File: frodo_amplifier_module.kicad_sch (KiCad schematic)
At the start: 38 parts, among them IC1 INA826AID, U1 ADC101C021CIMM, U2 MCP6001-OT, U3 MIC5504-3.3YM5, U4 REF3033

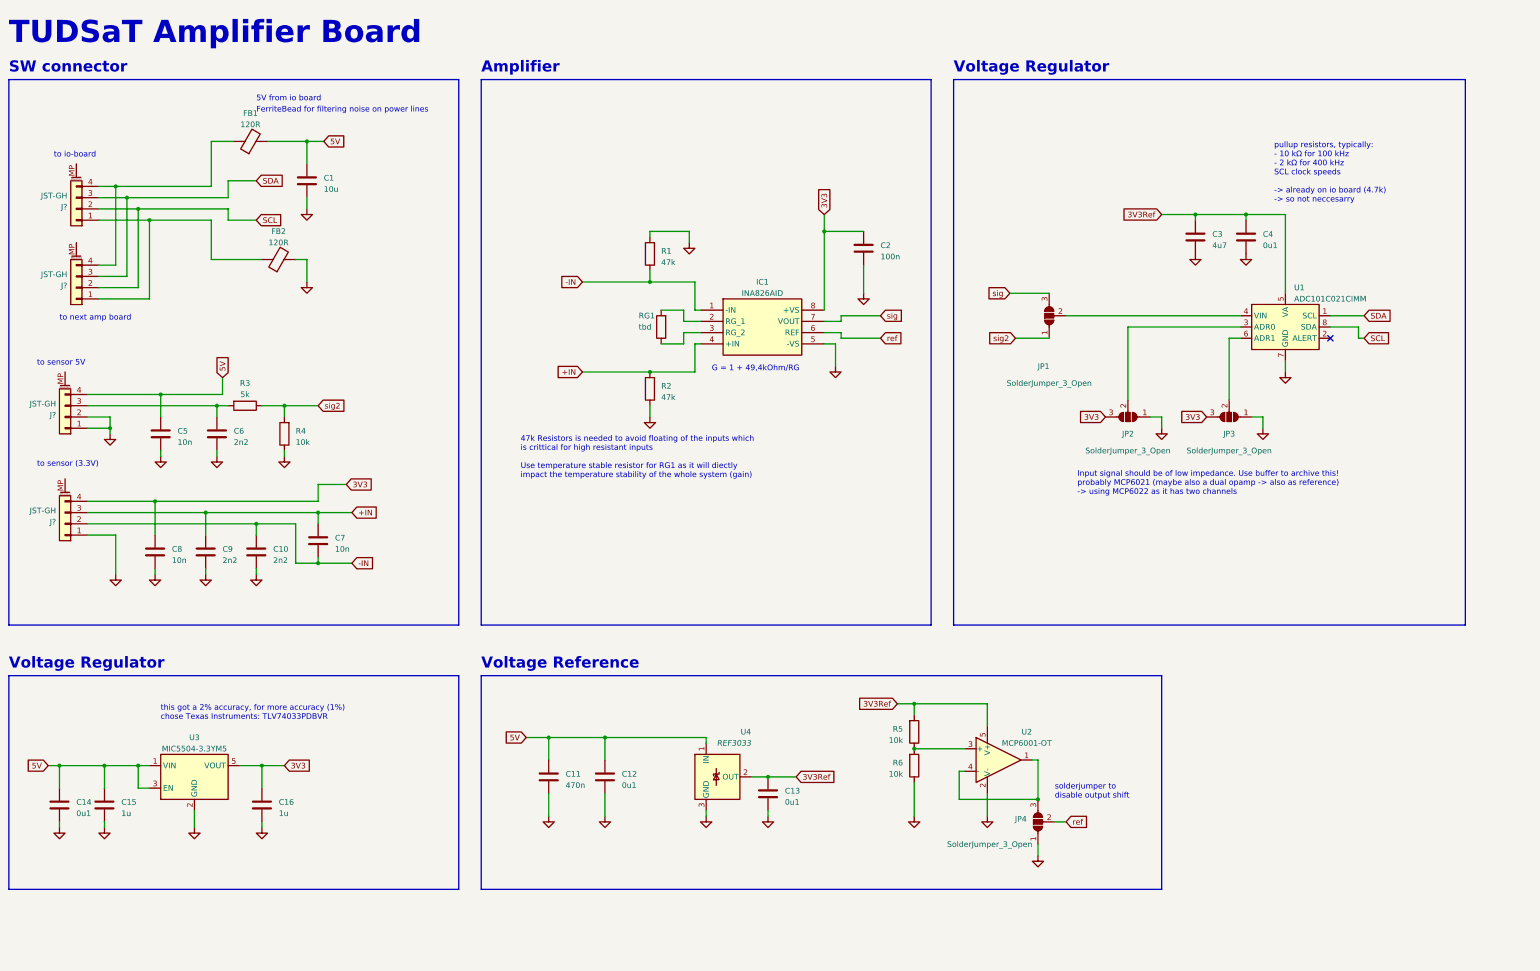
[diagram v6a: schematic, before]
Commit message: finished pcb layout - routing not done yet
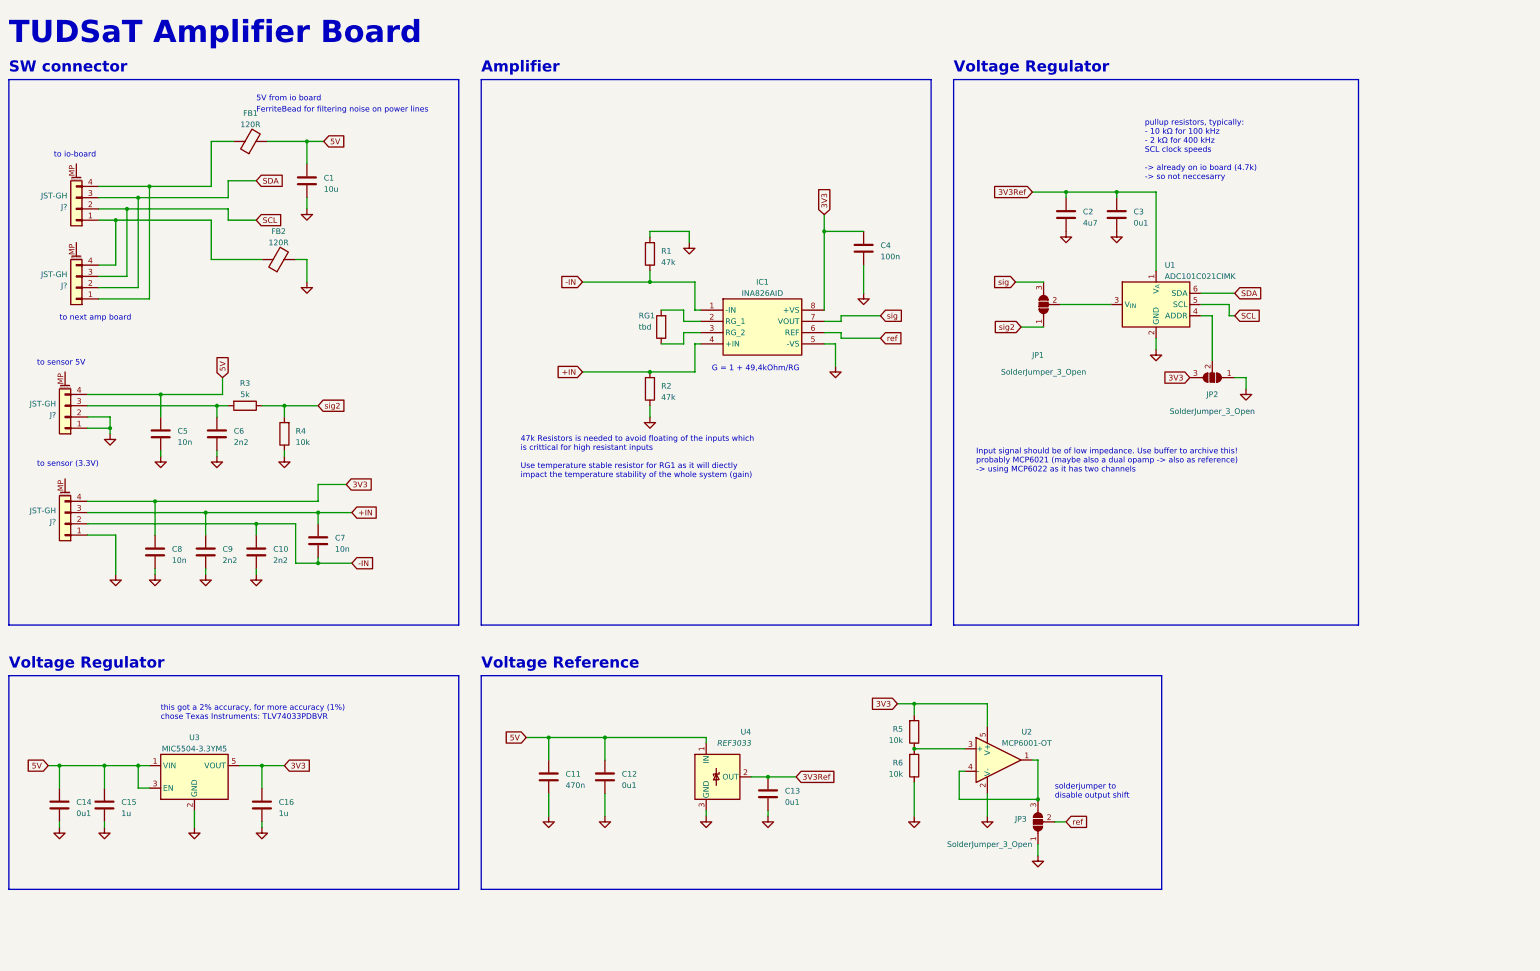
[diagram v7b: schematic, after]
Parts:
- removed JP2: SolderJumper_3_Open, Jumper:SolderJumper-3_P1.3mm_Open_RoundedPad1.0x1.5mm, symbol Jumper:SolderJumper_3_Open
- removed U1: ADC101C021CIMM, Package_SO:SSOP-8_2.95x2.8mm_P0.65mm, symbol Analog_ADC:ADC101C021CIMM
- added U1: ADC101C021CIMK, Package_TO_SOT_SMD:SOT-23-6, symbol Analog_ADC:ADC101C021CIMK
- renumbered C3 to C2, C4 to C3, C2 to C4, JP3 to JP2, JP4 to JP3
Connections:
- net 3V3: now also R5.2, U2.5 (V+)
- net 3V3Ref: now also U1.1 (V_{A}); no longer R5.2, U2.5 (V+)
- net GND: now also U1.2 (GND)
- net SCL: now also J?.3 (Pin_3), U1.5 (SCL); no longer J?.2 (Pin_2)
- net SDA: now also J?.2 (Pin_2), U1.6 (SDA); no longer J?.3 (Pin_3)
- net at JP1.2 (C): now also U1.3 (V_{IN})
- net at JP2.2 (C): now also U1.4 (ADDR)
- net at FB2.1, J?.1 (Pin_1): now also J?.4 (Pin_4); no longer J?.1 (Pin_1)
- net at FB1.1, J?.4 (Pin_4): now also J?.1 (Pin_1); no longer J?.4 (Pin_4)
- no-connect marks 1 -> 0
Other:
- moved on the sheet: C2, C3, JP1, JP2

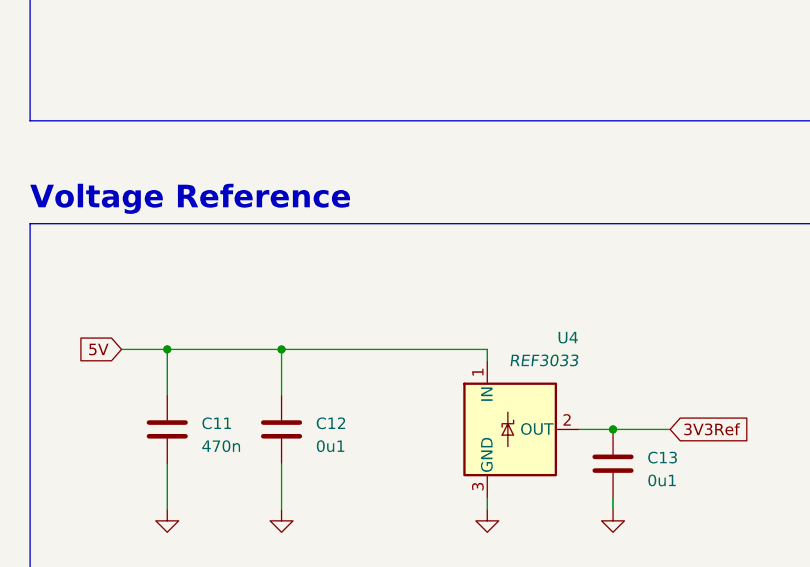
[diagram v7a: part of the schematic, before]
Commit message: optimised via placement
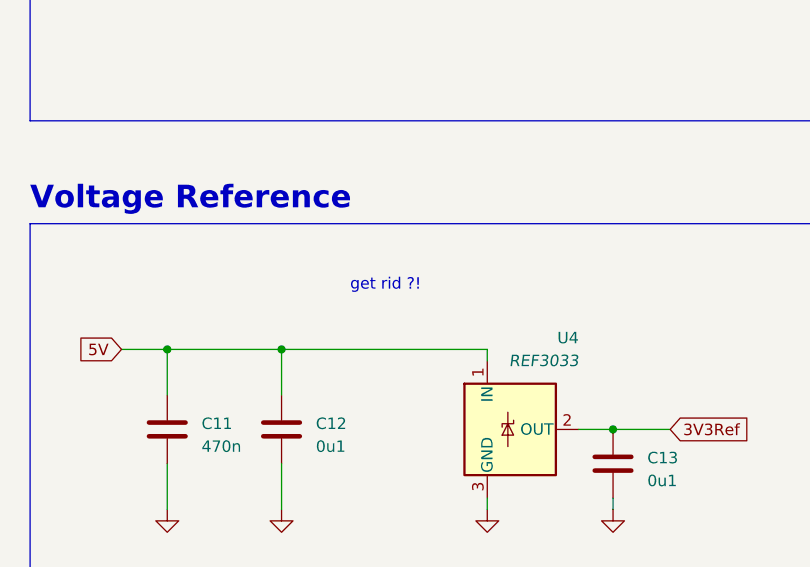
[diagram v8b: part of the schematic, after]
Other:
- note added: "get rid ?!"
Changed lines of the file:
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@@
     (effects (font (size 2.5 2.5) (thickness 0.5) bold) (justify left bottom))
+  )
+  (text "get rid ?!\n" (at 172.72 171.45 0)
+    (effects (font (size 1.27 1.27)) (justify left bottom))
   )
   (text "Voltage Regulator" (at 30.48 162.56 0)
